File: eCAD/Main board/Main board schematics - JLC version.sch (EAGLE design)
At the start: 65 parts, among them IC1 ESP32-WROOM-32E_M113EH3200PH3Q, IC2 TP4056X, IC3 DW01A-G, IC4 ME6211C33M5G-N, IC5 ME6211C33M5G-N, J1 XT30PW-M, Q1 IRF7319TRPBF, Q2 IRF7319TRPBF, Q3 SI2347DS-T1-GE3, Q4 FS8205A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

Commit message: Board for semestral project done
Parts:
- removed BOOT_N, ENABLE, FLASH, PSM_EINT_N, RESET_EN: (no value), switch-omron:31-XX
- removed J1: XT30PW-M, 1-component-search:XT30PW-M
- removed JP3: (no value), pinhead:PINHD-1X3
- removed JP5: (no value), pinhead:PINHD-1X2
- added BAT_IN: (no value), pinhead:PINHD-1X2
- added ESP_BOOT, ESP_RESET, NB_BOOT, NB_PSM, NB_RESET: TS-1088-AR02016, 1-component-search:TS-1088-AR02016
- added ESP_EN: (no value), pinhead:PINHD-1X3
- added SOLAR_IN: XT30PW-M, 1-component-search:XT30PW-M
- C12, C2: value 100u -> 220u
- C6: value 10u -> 100n; device rcl:C-EUC1206 -> rcl:C-EUC0805
- renumbered C11 to C2, JP2 to FAN, U2 to U1
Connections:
- net BAT+: now also BAT_IN.1; no longer JP5.1
- net BAT-: now also BAT_IN.2; no longer JP5.2
- net BOOT_N: now also NB_BOOT.NO; no longer BOOT_N.P
- net ESP_EN: now also ESP_EN.3, ESP_RESET.NO; no longer ENABLE.S, JP3.3
- net ESP_FLASH: now also ESP_BOOT.COM; no longer FLASH.S
- net GND: now also ESP_BOOT.NO, ESP_EN.1, ESP_EN.2, ESP_RESET.COM, SOLAR_IN.2, SOLAR_IN.3, SOLAR_IN.4; no longer ENABLE.P, FLASH.P, J1.2, J1.3, J1.4, JP3.1, JP3.2
- net PSM_EINT_N: now also NB_PSM.NO; no longer PSM_EINT_N.P
- net RESET_EN: now also NB_RESET.NO; no longer RESET_EN.P
- net VDD33: now also NB_BOOT.COM, NB_PSM.COM, NB_RESET.COM; no longer BOOT_N.S, PSM_EINT_N.S, RESET_EN.S
- net VIN: now also SOLAR_IN.1; no longer J1.1
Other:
- moved on the sheet: C14, C15, D2, R12, R18, R19, R20, SJ3, U$1

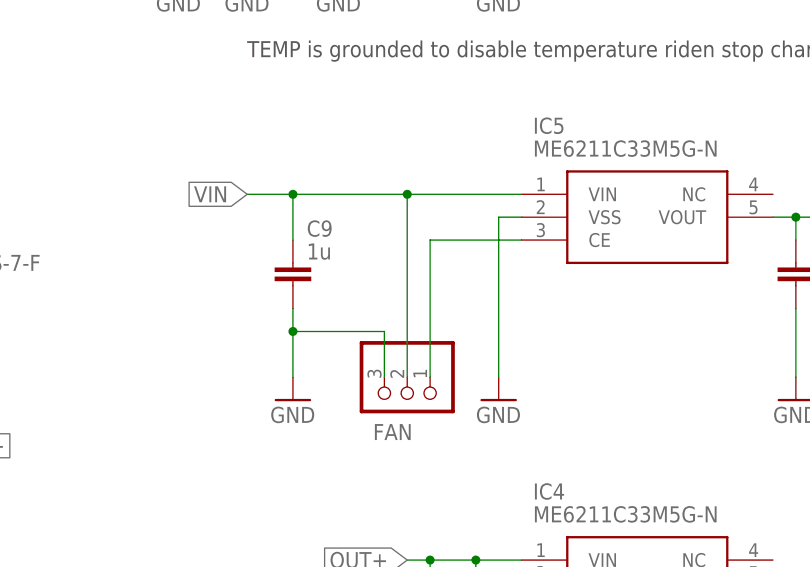
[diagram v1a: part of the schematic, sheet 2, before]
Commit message: Repair mistakes: C2, flash pin on ESP, fan pinout
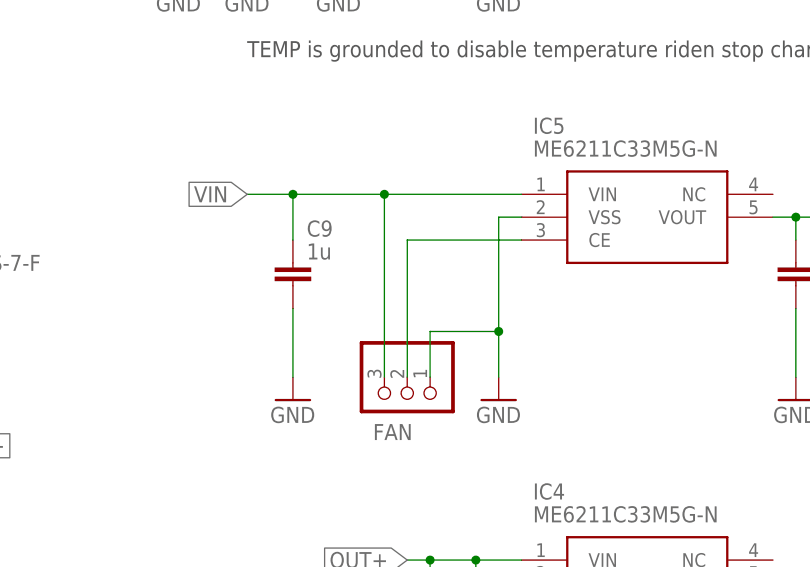
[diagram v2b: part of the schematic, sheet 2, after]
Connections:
- net ESP_FLASH: now also IC1.IO0; no longer IC1.IO2
- net GND: now also C2.-, FAN.1; no longer C2.+, FAN.3
- net N$6: now also FAN.2; no longer FAN.1
- net VDD33: now also C2.+; no longer C2.-
- net VIN: now also FAN.3; no longer FAN.2
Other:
- moved on the sheet: C2
